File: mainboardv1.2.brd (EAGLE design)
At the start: 79.7 x 80 mm, 128 parts, among them IC1 LM2596S, IC2 TDA2822D, IC3 MCP2562P, IC4 STM32F103RBT6, IC5 MIC2288YD5, IC6 ULN2003AD, IC7 LM2901, IC8 REG1117, IC9 SN74LVC1G10, Q1 8MHz

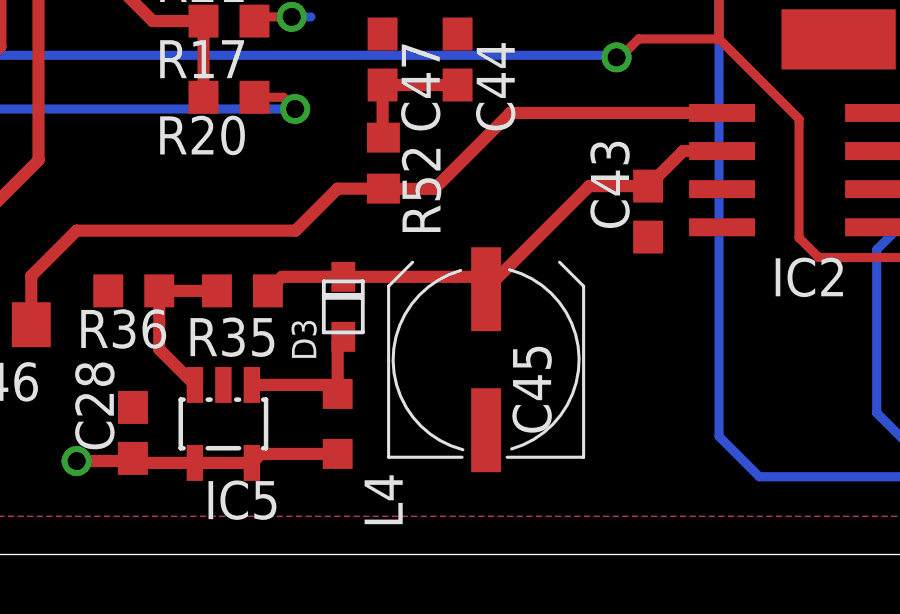
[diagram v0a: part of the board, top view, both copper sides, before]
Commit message: Small changed for compatibility with JLCPCBs parts library
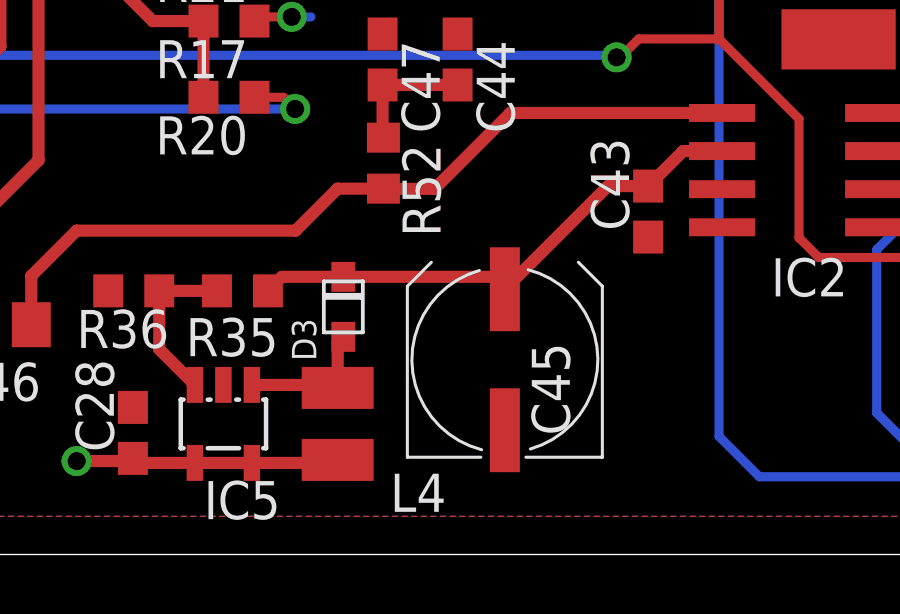
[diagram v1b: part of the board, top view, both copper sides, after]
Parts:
- L4: device rcl:L2012C -> rcl:L2825P
- moved C45 0.62 mm to (30.8, 6.49)
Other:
- board text added: "(c) 2020 Johannes Huebner"
- board text added: "openinverter.org"
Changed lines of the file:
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@@
 <text x="25.3125" y="22.8125" size="1.27" layer="25" rot="R90">openinverter.org main board rev 1.2</text>
 <text x="38.4375" y="54.6875" size="1.27" layer="25" rot="R180">(C) 2020 Johannes Huebner</text>
+<text x="73.125" y="67.8125" size="1.778" layer="30" font="vector" rot="MR0">(c) 2020 Johannes Huebner</text>
+<text x="58.4375" y="65.3125" size="1.778" layer="30" rot="MR0">openinverter.org</text>
 </plain>
 <attributes>
@@
 <element name="C37" library="rcl" package="C0603" value="22n" x="46.99" y="12.7" rot="R180"/>
 <element name="C43" library="rcl" package="C0603" value="1µ" x="35.56" y="11.43" rot="R90"/>
-<element name="C45" library="rcl" package="UD-6,3X7,7_NICHICON" value="470µ" x="30.16" y="6.4925" smashed="yes" rot="R90">
-<attribute name="NAME" x="32.3275" y="3.9725" size="1.27" layer="25" rot="R90"/>
-<attribute name="VALUE" x="32.7" y="5.2225" size="1.27" layer="27" rot="R90"/>
+<element name="C45" library="rcl" package="UD-6,3X7,7_NICHICON" value="470µ" x="30.785" y="6.4925" smashed="yes" rot="R90">
+<attribute name="NAME" x="32.9525" y="3.9725" size="1.27" layer="25" rot="R90"/>
+<attribute name="VALUE" x="33.325" y="5.2225" size="1.27" layer="27" rot="R90"/>
 </element>
 <element name="C1" library="rcl" package="C0805" value="10µ" x="9.5" y="7.62" rot="R180"/>
@@
 <element name="C47" library="rcl" package="C0603" value="22n" x="26.71" y="16.5" rot="R270"/>
 <element name="IC5" library="adafruit" package="SOT23-5L" value="MIC2288YD5" x="21.4025" y="4.3525" rot="R180"/>
-<element name="L4" library="rcl" package="L2012C" value="10µH" x="25.2125" y="4.3525" smashed="yes" rot="R90">
-<attribute name="NAME" x="27.38" y="0.855" size="1.27" layer="25" rot="R90"/>
+<element name="L4" library="rcl" package="L2825P" value="10µH" x="25.2125" y="4.3525" smashed="yes" rot="R90">
+<attribute name="NAME" x="28.8325" y="2.6925" size="1.27" layer="25" rot="R180"/>
 <attribute name="VALUE" x="27.7525" y="2.4475" size="1.27" layer="27" rot="R90"/>
 </element>
@@
 <contactref element="IC5" pad="4"/>
 <contactref element="L4" pad="1"/>
-<wire x1="22.3525" y1="3.0525" x2="22.6525" y2="3.3525" width="0.4064" layer="1"/>
-<wire x1="22.6525" y1="3.3525" x2="25.2125" y2="3.3525" width="0.4064" layer="1"/>
 <contactref element="C28" pad="1"/>
-<wire x1="25.2125" y1="3.3525" x2="25.3625" y2="3.2025" width="0.4064" layer="1"/>
+<wire x1="25.2125" y1="3.1525" x2="25.3625" y2="3.2025" width="0.4064" layer="1"/>
 <wire x1="18.3875" y1="3.2025" x2="18.3" y2="3.115" width="0.4064" layer="1"/>
 <wire x1="18.3" y1="3.115" x2="16.5125" y2="3.115" width="0.4064" layer="1"/>
@@
 <wire x1="5.0038" y1="50.165" x2="3.2025" y2="50.165" width="0.3048" layer="1"/>
 <wire x1="3.2025" y1="50.165" x2="2.8125" y2="49.775" width="0.3048" layer="1"/>
+<wire x1="22.3525" y1="3.0525" x2="25.2125" y2="3.0525" width="0.4064" layer="1"/>
+<wire x1="25.2125" y1="3.0525" x2="25.2125" y2="3.1525" width="0.4064" layer="1"/>
 </signal>
 <signal name="PA11/CANRX">
@@
 <wire x1="22.8875" y1="8.7875" x2="23.355" y2="9.255" width="0.4064" layer="1"/>
 <wire x1="23.355" y1="9.255" x2="25.4" y2="9.255" width="0.4064" layer="1"/>
-<wire x1="30.16" y1="8.8425" x2="29.7475" y2="9.255" width="0.4064" layer="1"/>
-<wire x1="29.7475" y1="9.255" x2="25.4" y2="9.255" width="0.4064" layer="1"/>
-<wire x1="30.16" y1="8.8425" x2="33.5975" y2="12.28" width="0.4064" layer="1"/>
-<wire x1="33.5975" y1="12.28" x2="35.56" y2="12.28" width="0.4064" layer="1"/>
+<wire x1="30.785" y1="8.8425" x2="30.685" y2="9.255" width="0.4064" layer="1"/>
+<wire x1="30.685" y1="9.255" x2="25.4" y2="9.255" width="0.4064" layer="1"/>
+<wire x1="30.785" y1="8.8425" x2="34.2225" y2="12.28" width="0.4064" layer="1"/>
+<wire x1="34.2225" y1="12.28" x2="35.56" y2="12.28" width="0.4064" layer="1"/>
 <contactref element="IC2" pad="2"/>
 <wire x1="36.7275" y1="13.4475" x2="38.025" y2="13.4475" width="0.4064" layer="1"/>
@@
 <contactref element="IC5" pad="1"/>
 <wire x1="22.3525" y1="5.6525" x2="24.9125" y2="5.6525" width="0.4064" layer="1"/>
-<wire x1="24.9125" y1="5.6525" x2="25.2125" y2="5.3525" width="0.4064" layer="1"/>
+<wire x1="24.9125" y1="5.6525" x2="25.2125" y2="5.5525" width="0.4064" layer="1"/>
 <contactref element="D3" pad="A"/>
 <wire x1="25.4" y1="7.255" x2="25.2125" y2="7.0675" width="0.4064" layer="1"/>
-<wire x1="25.2125" y1="7.0675" x2="25.2125" y2="5.3525" width="0.4064" layer="1"/>
+<wire x1="25.2125" y1="7.0675" x2="25.2125" y2="5.5525" width="0.4064" layer="1"/>
 </signal>
 <signal name="N$27">

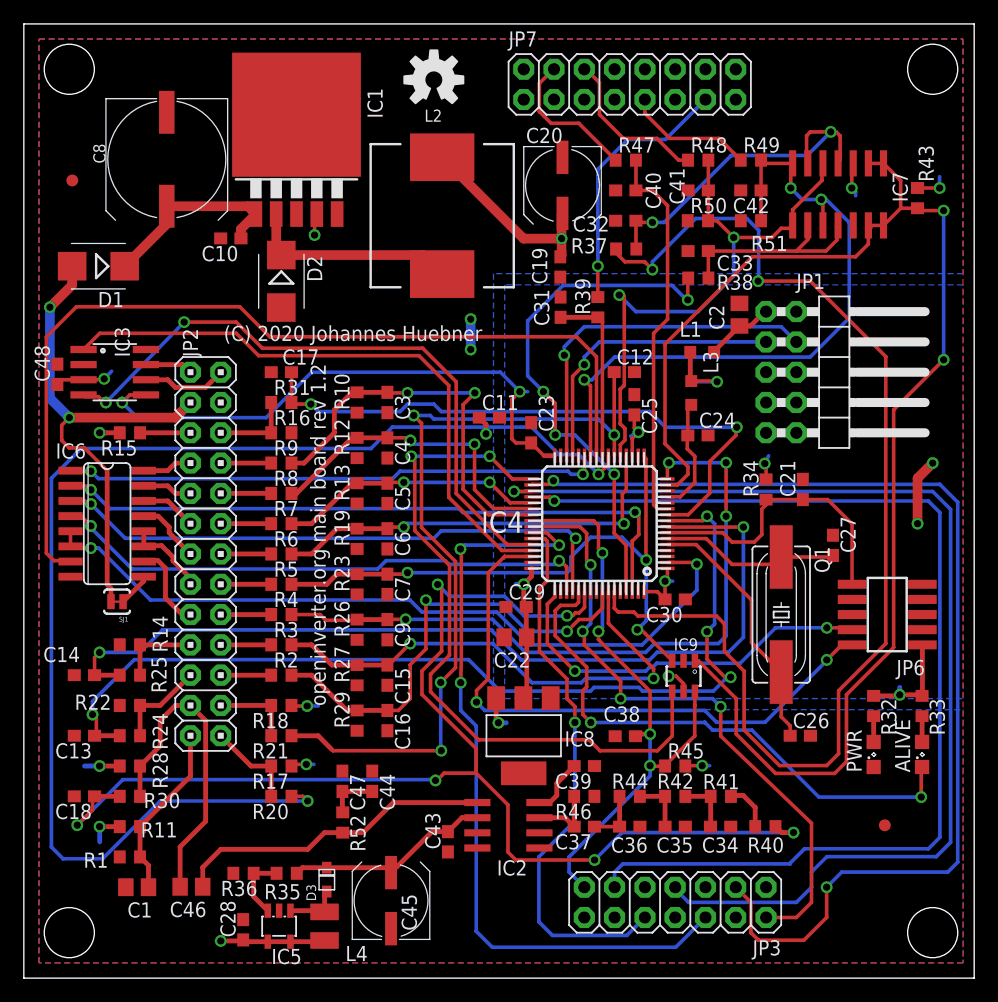
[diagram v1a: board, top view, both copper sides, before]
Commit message: Replaced SOT23-6 by SC70-6 foot print for IC9 Moved copyright info away from trace fixed font of silk screen
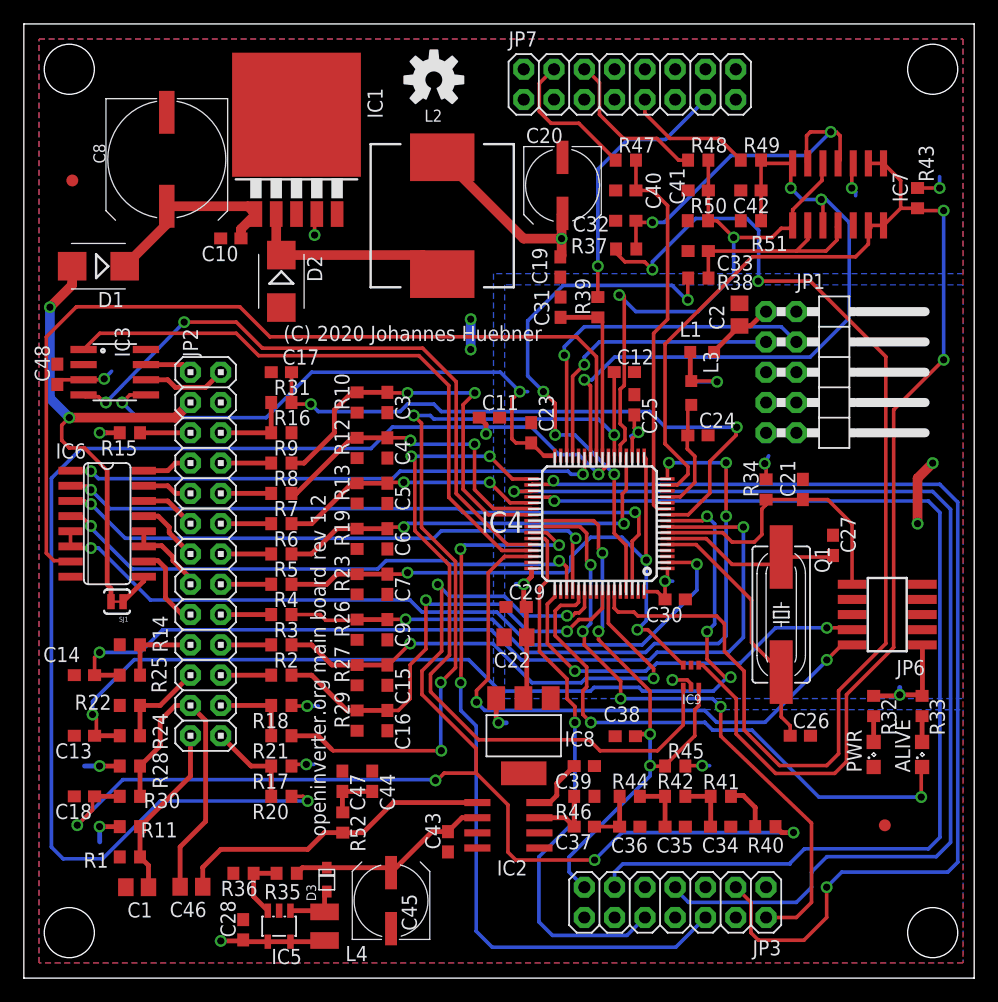
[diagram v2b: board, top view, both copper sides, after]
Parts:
- IC9: value SN74LVC1G10 -> NC7SZ10P6X; device 74xx-eu:SOT23-6 -> 74xx-eu:SC70-6
- moved IC9 0.62 mm to (55.9, 25.3), turned to 180 degrees
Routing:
- net PA3/ADC3: track 52.1 -> 53.5 mm
- net PB12/TIM1_BKIN: track 59.3 -> 60.1 mm
- net PC9: track 51.4 -> 51.9 mm
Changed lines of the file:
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@@
 <layer number="28" name="bValues" color="7" fill="1" visible="no" active="yes"/>
 <layer number="29" name="tStop" color="7" fill="3" visible="no" active="yes"/>
-<layer number="30" name="bStop" color="7" fill="6" visible="no" active="yes"/>
+<layer number="30" name="bStop" color="7" fill="6" visible="yes" active="yes"/>
 <layer number="31" name="tCream" color="7" fill="4" visible="no" active="yes"/>
 <layer number="32" name="bCream" color="7" fill="5" visible="no" active="yes"/>
@@
 <hole x="3.81" y="3.81" drill="4.2"/>
 <hole x="76.2" y="3.81" drill="4.2"/>
-<text x="25.3125" y="22.8125" size="1.27" layer="25" rot="R90">openinverter.org main board rev 1.2</text>
-<text x="38.4375" y="54.6875" size="1.27" layer="25" rot="R180">(C) 2020 Johannes Huebner</text>
-<text x="73.125" y="67.8125" size="1.778" layer="30" font="vector" rot="MR0">(c) 2020 Johannes Huebner</text>
-<text x="58.4375" y="65.3125" size="1.778" layer="30" rot="MR0">openinverter.org</text>
+<text x="25.3125" y="11.875" size="1.27" layer="25" font="vector" rot="R90">openinverter.org main board rev 1.2</text>
+<text x="43.4375" y="54.6875" size="1.27" layer="25" font="vector" rot="R180">(C) 2020 Johannes Huebner</text>
+<text x="46.5625" y="68.125" size="1.778" layer="30" font="vector" rot="MR0">(c) 2020 Johannes Huebner</text>
+<text x="30.625" y="65" size="1.778" layer="30" font="vector" rot="MR0">openinverter.org</text>
 </plain>
 <attributes>
@@
 <attribute name="VALUE" x="46.905" y="55.615" size="1.27" layer="27" rot="R90"/>
 </element>
-<element name="IC9" library="74xx-eu" package="SOT23-6" value="SN74LVC1G10" x="55.3125" y="25.3125" smashed="yes">
-<attribute name="NAME" x="54.487" y="27.4715" size="1.016" layer="25"/>
-<attribute name="VALUE" x="54.36" y="25.122" size="0.4064" layer="27"/>
-</element>
 <element name="C48" library="rcl" package="C0603" value="1µ" x="2.8125" y="50.625" rot="R90"/>
 <element name="LOGO1" library="SparkFun-Aesthetics" package="OSHW-LOGO-M" value="OSHW-LOGOM" x="34.375" y="75.3125"/>
 <element name="SJ1" library="SparkFun-Passives" package="SJ_2S-TRACE" value="SOLDERJUMPERTRACE" x="7.8125" y="31.5625" rot="R180"/>
+<element name="IC9" library="74xx-eu" package="SC70-6" value="NC7SZ10P6X" x="55.9375" y="25.3125" smashed="yes" rot="R180">
+<attribute name="NAME" x="56.8265" y="23.7885" size="0.8128" layer="25" rot="R180"/>
+<attribute name="VALUE" x="56.6995" y="25.5665" size="0.4064" layer="27" rot="R180"/>
+</element>
 </elements>
 <signals>
@@
 <contactref element="R14" pad="1"/>
 <contactref element="C1" pad="2"/>
-<contactref element="IC9" pad="2"/>
-<contactref element="IC9" pad="2"/>
 <contactref element="C26" pad="2"/>
 <contactref element="C27" pad="2"/>
@@
 <contactref element="C39" pad="1"/>
 <contactref element="C48" pad="2"/>
+<contactref element="IC9" pad="2"/>
+<contactref element="IC9" pad="2"/>
 </signal>
 <signal name="VCC">
@@
 <wire x1="47.3875" y1="19.9825" x2="48.3075" y2="19.0625" width="0.3048" layer="1"/>
 <wire x1="48.3075" y1="19.0625" x2="53.125" y2="19.0625" width="0.3048" layer="1"/>
-<wire x1="53.125" y1="19.0625" x2="54.3625" y2="20.3" width="0.3048" layer="1"/>
+<wire x1="53.125" y1="19.0625" x2="55.2875" y2="21.225" width="0.3048" layer="1"/>
 <contactref element="IC9" pad="4"/>
-<wire x1="54.3625" y1="20.3" x2="54.3625" y2="24.0124" width="0.3048" layer="1"/>
+<wire x1="55.2875" y1="21.225" x2="55.2875" y2="24.3875" width="0.3048" layer="1"/>
 </signal>
 <signal name="TIM1_CH1N">
@@
 <wire x1="52.505" y1="17.8125" x2="52.57" y2="17.7475" width="0.3048" layer="1"/>
 <wire x1="52.57" y1="17.7475" x2="53.76" y2="17.78" width="0.3048" layer="1"/>
-<wire x1="56.25" y1="22.8549" x2="56.25" y2="20.3125" width="0.3048" layer="1"/>
 <wire x1="56.25" y1="20.3125" x2="53.76" y2="17.8225" width="0.3048" layer="1"/>
 <wire x1="53.76" y1="17.8225" x2="53.76" y2="17.78" width="0.3048" layer="1"/>
@@
 <wire x1="51.4575" y1="20.46" x2="52.505" y2="20.46" width="0.4064" layer="1"/>
 <contactref element="IC9" pad="6"/>
-<wire x1="56.25" y1="22.8549" x2="56.2625" y2="22.8674" width="0.3048" layer="1"/>
-<wire x1="56.2625" y1="22.8674" x2="56.2625" y2="24.0124" width="0.3048" layer="1"/>
+<wire x1="56.5875" y1="22.8375" x2="56.5875" y2="24.3875" width="0.3048" layer="1"/>
+<wire x1="56.25" y1="20.3125" x2="56.25" y2="22.5" width="0.3048" layer="1"/>
+<wire x1="56.25" y1="22.5" x2="56.5875" y2="22.8375" width="0.3048" layer="1"/>
 </signal>
 <signal name="PC10">
@@
 <wire x1="72.93" y1="47.65" x2="77.12" y2="51.84" width="0.3048" layer="1"/>
 <wire x1="53.76" y1="53.16" x2="61.08" y2="60.48" width="0.3048" layer="1"/>
-<wire x1="59.73" y1="23.43" x2="56.5474" y2="26.6126" width="0.3048" layer="1"/>
 <contactref element="IC9" pad="1"/>
-<wire x1="56.5474" y1="26.6126" x2="56.2625" y2="26.6126" width="0.3048" layer="1"/>
+<wire x1="59.73" y1="23.43" x2="56.9225" y2="26.2375" width="0.3048" layer="1"/>
+<wire x1="56.9225" y1="26.2375" x2="56.5875" y2="26.2375" width="0.3048" layer="1"/>
 </signal>
 <signal name="UDC">
@@
 <via x="51.435" y="29.21" extent="1-16" drill="0.6" shape="octagon"/>
 <wire x1="51.435" y1="29.21" x2="51.7351" y2="29.21" width="0.3048" layer="1"/>
+<wire x1="51.7651" y1="29.21" x2="51.435" y2="29.21" width="0.3048" layer="1"/>
 <contactref element="IC9" pad="3"/>
-<wire x1="54.3625" y1="26.6126" x2="51.7651" y2="29.21" width="0.3048" layer="1"/>
-<wire x1="51.7651" y1="29.21" x2="51.435" y2="29.21" width="0.3048" layer="1"/>
+<wire x1="55.2875" y1="26.2375" x2="52.315" y2="29.21" width="0.3048" layer="1"/>
+<wire x1="52.315" y1="29.21" x2="51.435" y2="29.21" width="0.3048" layer="1"/>
 </signal>
 <signal name="N$10">
@@
 <wire x1="55.875" y1="50.06" x2="55.875" y2="52.5" width="0.4064" layer="1"/>
 <contactref element="IC9" pad="5"/>
-<wire x1="55.3125" y1="24.0124" x2="55.3125" y2="24.6875" width="0.3048" layer="1"/>
-<wire x1="55.3125" y1="24.6875" x2="54.6875" y2="25.3125" width="0.3048" layer="1"/>
-<wire x1="54.6875" y1="25.3125" x2="54.0625" y2="25.3125" width="0.3048" layer="1"/>
-<via x="54.0625" y="25.3125" extent="1-16" drill="0.6" shape="octagon"/>
-<wire x1="54.0625" y1="25.3125" x2="54.375" y2="25.3125" width="0.3048" layer="16"/>
+<wire x1="55.9375" y1="24.3875" x2="55.9375" y2="24.6875" width="0.3048" layer="1"/>
+<wire x1="55.9375" y1="24.6875" x2="55.625" y2="25" width="0.3048" layer="1"/>
+<wire x1="55.625" y1="25" x2="54.375" y2="25" width="0.3048" layer="1"/>
+<via x="54.375" y="25" extent="1-16" drill="0.6" shape="octagon"/>
+<wire x1="54.375" y1="25" x2="54.375" y2="25.3125" width="0.3048" layer="16"/>
 </signal>
 <signal name="NRST">
